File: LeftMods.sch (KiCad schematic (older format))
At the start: 8 parts

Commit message: Clean up some files
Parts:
- removed D60, D61, D62: D_Small, Diodes_SMD:D_SOD-123, symbol D_Small
- removed LM1, LM4: MX-1.5U, MX_Alps_Hybrid:MX-1.5U, symbol MX-1U
- removed LM2: MX-1U, MX_Alps_Hybrid:MX-1U, symbol MX-1U
- removed LM3: MX-1.25U, MX_Alps_Hybrid:MX-1.25U-FLIPPED, symbol MX-1U
- removed LM5: MX-1.5U, MX_Alps_Hybrid:MX-1.5U-FLIPPED, symbol MX-1U
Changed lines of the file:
@@
 LIBS:logic
 LIBS:Type-C
-LIBS:VoyagerII-cache
+LIBS:Voyager65-cache
 EELAYER 25 0
 EELAYER END
@@
 Comment4 ""
 $EndDescr
-$Comp
-L MX-1U LM1
-U 1 1 5A68E95B
-P 2325 2225
-F 0 "LM1" H 2325 2350 60  0000 C CNN
-F 1 "MX-1.5U" H 2325 2275 20  0000 C CNN
-F 2 "MX_Alps_Hybrid:MX-1.5U" H 2300 2200 60  0001 C CNN
-F 3 "" H 2300 2200 60  0001 C CNN
-	1    2325 2225
-	1    0    0    -1
-$EndComp
-$Comp
-L D_Small D60
-U 1 1 5A68E962
-P 2225 2500
-F 0 "D60" H 2175 2580 50  0000 L CNN
-F 1 "D_Small" H 2075 2420 50  0000 L CNN
-F 2 "Diodes_SMD:D_SOD-123" V 2225 2500 50  0001 C CNN
-F 3 "" V 2225 2500 50  0001 C CNN
-	1    2225 2500
-	0    -1   -1   0
-$EndComp
-$Comp
-L MX-1U LM2
-U 1 1 5A68E96A
-P 2775 2225
-F 0 "LM2" H 2775 2350 60  0000 C CNN
-F 1 "MX-1U" H 2775 2275 20  0000 C CNN
-F 2 "MX_Alps_Hybrid:MX-1U" H 2750 2200 60  0001 C CNN
-F 3 "" H 2750 2200 60  0001 C CNN
-	1    2775 2225
-	1    0    0    -1
-$EndComp
-$Comp
-L D_Small D61
-U 1 1 5A68E971
-P 2675 2500
-F 0 "D61" H 2625 2580 50  0000 L CNN
-F 1 "D_Small" H 2525 2420 50  0000 L CNN
-F 2 "Diodes_SMD:D_SOD-123" V 2675 2500 50  0001 C CNN
-F 3 "" V 2675 2500 50  0001 C CNN
-	1    2675 2500
-	0    -1   -1   0
-$EndComp
-Wire Wire Line
-	2600 2400 2750 2400
-$Comp
-L MX-1U LM4
-U 1 1 5A68E979
-P 3225 2225
-F 0 "LM4" H 3225 2350 60  0000 C CNN
-F 1 "MX-1.5U" H 3225 2275 20  0000 C CNN
-F 2 "MX_Alps_Hybrid:MX-1.5U" H 3200 2200 60  0001 C CNN
-F 3 "" H 3200 2200 60  0001 C CNN
-	1    3225 2225
-	1    0    0    -1
-$EndComp
-$Comp
-L D_Small D62
-U 1 1 5A68E980
-P 3125 2500
-F 0 "D62" H 3075 2580 50  0000 L CNN
-F 1 "D_Small" H 2975 2420 50  0000 L CNN
-F 2 "Diodes_SMD:D_SOD-123" V 3125 2500 50  0001 C CNN
-F 3 "" V 3125 2500 50  0001 C CNN
-	1    3125 2500
-	0    -1   -1   0
-$EndComp
-Wire Wire Line
-	3125 2400 3525 2400
-$Comp
-L MX-1U LM3
-U 1 1 5A68E997
-P 2775 2850
-F 0 "LM3" H 2775 2975 60  0000 C CNN
-F 1 "MX-1.25U" H 2775 2900 20  0000 C CNN
-F 2 "MX_Alps_Hybrid:MX-1.25U-FLIPPED" H 2750 2825 60  0001 C CNN
-F 3 "" H 2750 2825 60  0001 C CNN
-	1    2775 2850
-	1    0    0    -1
-$EndComp
-Wire Wire Line
-	2600 3025 2750 3025
-$Comp
-L MX-1U LM5
-U 1 1 5A68E9A6
-P 3225 2850
-F 0 "LM5" H 3225 2975 60  0000 C CNN
-F 1 "MX-1.5U" H 3225 2900 20  0000 C CNN
-F 2 "MX_Alps_Hybrid:MX-1.5U-FLIPPED" H 3200 2825 60  0001 C CNN
-F 3 "" H 3200 2825 60  0001 C CNN
-	1    3225 2850
-	1    0    0    -1
-$EndComp
-Connection ~ 3125 2400
-Wire Wire Line
-	2600 2400 2600 3025
-Connection ~ 2675 2400
-Text GLabel 2500 1700 1    60   Input ~ 0
-COL0
-Wire Wire Line
-	2950 1700 2950 2825
-Text GLabel 2950 1700 1    60   Input ~ 0
-COL1
-Wire Wire Line
-	3400 1700 3400 2675
-Text GLabel 3400 1700 1    60   Input ~ 0
-COL2
-Wire Wire Line
-	1700 2600 3125 2600
-Text GLabel 1700 2600 0    60   Input ~ 0
-ROW4
-Connection ~ 2225 2600
-Connection ~ 2675 2600
-Connection ~ 2950 2200
-Connection ~ 3400 2200
-Connection ~ 2800 2350
-Wire Wire Line
-	2500 1700 2500 2200
-Wire Wire Line
-	2225 2400 2300 2400
-Wire Wire Line
-	3400 2675 3200 2675
-Wire Wire Line
-	3200 2675 3200 3025
-Wire Wire Line
-	3525 2825 3400 2825
-Connection ~ 3200 2400
-Wire Wire Line
-	3525 2400 3525 2825
-Wire Wire Line
-	1750 2350 3250 2350
-Connection ~ 2350 2350
-Text GLabel 1750 2350 0    60   Input ~ 0
-LED-SW1
-Wire Wire Line
-	2450 2250 2450 1325
-Text GLabel 2450 1325 1    60   Input ~ 0
-LED-CS1
-Wire Wire Line
-	2900 1325 2900 2875
-Text GLabel 2900 1325 1    60   Input ~ 0
-LED-CS2
-Wire Wire Line
-	3350 1325 3350 2875
-Text GLabel 3350 1325 1    60   Input ~ 0
-LED-CS3
-Connection ~ 2900 2250
-Wire Wire Line
-	2800 2350 2800 2975
-Connection ~ 3350 2250
-Wire Wire Line
-	3250 2350 3250 2975
 $EndSCHEMATC

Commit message: Replace MCU, route bus
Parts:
- added D63, D64, D65: D_Small, Diodes_SMD:D_SOD-123, symbol D_Small
- added K_LM1, K_LM7: MX-1.5U, MX_Alps_Hybrid:MX-1.5U, symbol MX-1.5U
- added K_LM2: MX-1.25U, MX_Alps_Hybrid:MX-1.25U-FLIPPED, symbol MX-1.5U
- added K_LM3: MX-1.5U, MX_Alps_Hybrid:MX-1.5U-FLIPPED, symbol MX-1.5U
- added K_LM4, K_LM5, K_LM6: MX-1.25U, MX_Alps_Hybrid:MX-1.25U, symbol MX-1.5U
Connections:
- new net: D63.2 (A), K_LM1.2 (ROW)
- new net: D64.2 (A), K_LM3.2 (ROW), K_LM4.1 (COL)
- new net: D65.2 (A), K_LM6.2 (ROW), K_LM7.1 (COL)
- new net COL0: K_LM1.1 (COL), K_LM2.1 (COL)
- new net COL1: K_LM3.1 (COL), K_LM4.2 (ROW), K_LM5.1 (COL)
- new net COL2: K_LM6.1 (COL), K_LM7.2 (ROW)
- new net ROW4: D63.1 (K), D64.1 (K), D65.1 (K)
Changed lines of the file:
@@
 $Descr A4 11693 8268
 encoding utf-8
-Sheet 4 6
+Sheet 3 6
 Title ""
 Date ""
@@
 Comment4 ""
 $EndDescr
+$Comp
+L MX-1.5U K_LM1
+U 1 1 5ACD9BDC
+P 2225 2600
+F 0 "K_LM1" H 2225 2725 60  0000 C CNN
+F 1 "MX-1.5U" H 2225 2650 20  0000 C CNN
+F 2 "MX_Alps_Hybrid:MX-1.5U" H 2200 2575 60  0001 C CNN
+F 3 "" H 2200 2575 60  0001 C CNN
+	1    2225 2600
+	1    0    0    -1
+$EndComp
+$Comp
+L MX-1.5U K_LM2
+U 1 1 5ACD9C06
+P 2225 3200
+F 0 "K_LM2" H 2225 3325 60  0000 C CNN
+F 1 "MX-1.25U" H 2225 3250 20  0000 C CNN
+F 2 "MX_Alps_Hybrid:MX-1.25U-FLIPPED" H 2200 3175 60  0001 C CNN
+F 3 "" H 2200 3175 60  0001 C CNN
+	1    2225 3200
+	1    0    0    -1
+$EndComp
+$Comp
+L D_Small D63
+U 1 1 5ACD9CD9
+P 2125 2875
+F 0 "D63" H 2075 2955 50  0000 L CNN
+F 1 "D_Small" H 1975 2795 50  0000 L CNN
+F 2 "Diodes_SMD:D_SOD-123" V 2125 2875 50  0001 C CNN
+F 3 "" V 2125 2875 50  0001 C CNN
+	1    2125 2875
+	0    -1   -1   0
+$EndComp
+$Comp
+L MX-1.5U K_LM3
+U 1 1 5ACDA08B
+P 2750 2600
+F 0 "K_LM3" H 2750 2725 60  0000 C CNN
+F 1 "MX-1.5U" H 2750 2650 20  0000 C CNN
+F 2 "MX_Alps_Hybrid:MX-1.5U-FLIPPED" H 2725 2575 60  0001 C CNN
+F 3 "" H 2725 2575 60  0001 C CNN
+	1    2750 2600
+	1    0    0    -1
+$EndComp
+$Comp
+L MX-1.5U K_LM4
+U 1 1 5ACDA091
+P 2750 3200
+F 0 "K_LM4" H 2750 3325 60  0000 C CNN
+F 1 "MX-1.25U" H 2750 3250 20  0000 C CNN
+F 2 "MX_Alps_Hybrid:MX-1.25U" H 2725 3175 60  0001 C CNN
+F 3 "" H 2725 3175 60  0001 C CNN
+	1    2750 3200
+	1    0    0    -1
+$EndComp
+$Comp
+L D_Small D64
+U 1 1 5ACDA097
+P 2650 2875
+F 0 "D64" H 2600 2955 50  0000 L CNN
+F 1 "D_Small" H 2500 2795 50  0000 L CNN
+F 2 "Diodes_SMD:D_SOD-123" V 2650 2875 50  0001 C CNN
+F 3 "" V 2650 2875 50  0001 C CNN
+	1    2650 2875
+	0    -1   -1   0
+$EndComp
+$Comp
+L MX-1.5U K_LM5
+U 1 1 5ACDA0FC
+P 2750 3800
+F 0 "K_LM5" H 2750 3925 60  0000 C CNN
+F 1 "MX-1.25U" H 2750 3850 20  0000 C CNN
+F 2 "MX_Alps_Hybrid:MX-1.25U" H 2725 3775 60  0001 C CNN
+F 3 "" H 2725 3775 60  0001 C CNN
+	1    2750 3800
+	1    0    0    -1
+$EndComp
+$Comp
+L MX-1.5U K_LM6
+U 1 1 5ACDA22D
+P 3350 2600
+F 0 "K_LM6" H 3350 2725 60  0000 C CNN
+F 1 "MX-1.25U" H 3350 2650 20  0000 C CNN
+F 2 "MX_Alps_Hybrid:MX-1.25U" H 3325 2575 60  0001 C CNN
+F 3 "" H 3325 2575 60  0001 C CNN
+	1    3350 2600
+	1    0    0    -1
+$EndComp
+$Comp
+L MX-1.5U K_LM7
+U 1 1 5ACDA233
+P 3350 3200
+F 0 "K_LM7" H 3350 3325 60  0000 C CNN
+F 1 "MX-1.5U" H 3350 3250 20  0000 C CNN
+F 2 "MX_Alps_Hybrid:MX-1.5U" H 3325 3175 60  0001 C CNN
+F 3 "" H 3325 3175 60  0001 C CNN
+	1    3350 3200
+	1    0    0    -1
+$EndComp
+$Comp
+L D_Small D65
+U 1 1 5ACDA239
+P 3250 2875
+F 0 "D65" H 3200 2955 50  0000 L CNN
+F 1 "D_Small" H 3100 2795 50  0000 L CNN
+F 2 "Diodes_SMD:D_SOD-123" V 3250 2875 50  0001 C CNN
+F 3 "" V 3250 2875 50  0001 C CNN
+	1    3250 2875
+	0    -1   -1   0
+$EndComp
+Text GLabel 1925 2975 0    60   Input ~ 0
+ROW4
+Text GLabel 2400 2300 1    60   Input ~ 0
+COL0
+Text GLabel 2925 2300 1    60   Input ~ 0
+COL1
+Text GLabel 3525 2300 1    60   Input ~ 0
+COL2
+Connection ~ 3525 2575
+Connection ~ 2925 2575
+Wire Wire Line
+	2925 2300 2925 3125
+Wire Wire Line
+	2925 3225 2925 3775
+Connection ~ 2400 2575
+Wire Wire Line
+	2400 2300 2400 3175
+Connection ~ 2125 2975
+Connection ~ 2650 2975
+Wire Wire Line
+	1925 2975 3250 2975
+Wire Wire Line
+	3250 2775 3600 2775
+Wire Wire Line
+	2650 2775 2750 2775
+Wire Wire Line
+	2125 2775 2200 2775
+Wire Wire Line
+	3525 2300 3525 3075
+Wire Wire Line
+	3525 3075 3325 3075
+Wire Wire Line
+	3325 3075 3325 3375
+Wire Wire Line
+	3525 3175 3600 3175
+Wire Wire Line
+	3600 3175 3600 2775
+Connection ~ 3325 2775
+Wire Wire Line
+	2925 3125 2975 3125
+Wire Wire Line
+	2975 3125 2975 3225
+Wire Wire Line
+	2975 3225 2925 3225
+Wire Wire Line
+	2925 3175 2750 3175
+Wire Wire Line
+	2750 3175 2750 2775
+Connection ~ 2725 2775
+Wire Wire Line
+	2725 3375 2925 3375
+Connection ~ 2925 3375
 $EndSCHEMATC

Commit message: Temporary progress save
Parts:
- K_LM4: footprint MX_Alps_Hybrid:MX-1.25U -> MX_Alps_Hybrid:MX-1.25U-FLIPPED
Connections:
- net at D64.2 (A), K_LM3.2 (ROW), K_LM4.1 (COL): now also K_LM5.2 (ROW)
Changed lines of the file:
@@
 F 0 "K_LM4" H 2750 3325 60  0000 C CNN
 F 1 "MX-1.25U" H 2750 3250 20  0000 C CNN
-F 2 "MX_Alps_Hybrid:MX-1.25U" H 2725 3175 60  0001 C CNN
+F 2 "MX_Alps_Hybrid:MX-1.25U-FLIPPED" H 2725 3175 60  0001 C CNN
 F 3 "" H 2725 3175 60  0001 C CNN
 	1    2750 3200
@@
 	3250 2775 3600 2775
 Wire Wire Line
-	2650 2775 2750 2775
+	2525 2775 2750 2775
 Wire Wire Line
 	2125 2775 2200 2775
@@
 	2725 3375 2925 3375
 Connection ~ 2925 3375
+Wire Wire Line
+	2725 3975 2725 3475
+Wire Wire Line
+	2725 3475 2525 3475
+Wire Wire Line
+	2525 3475 2525 2775
+Connection ~ 2650 2775
 $EndSCHEMATC

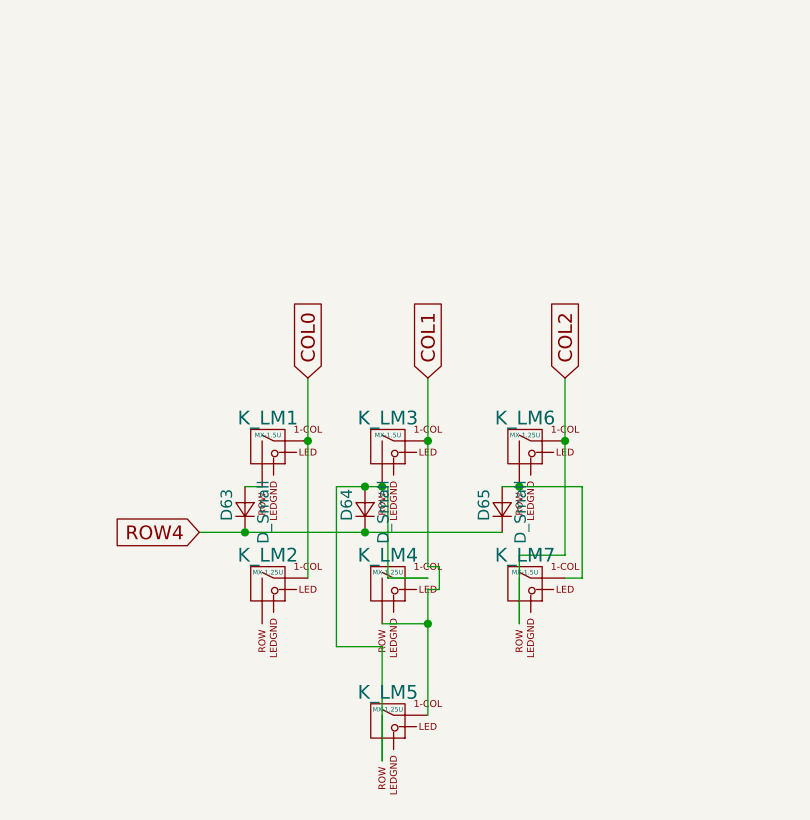
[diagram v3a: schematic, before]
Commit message: Finish project basic routing
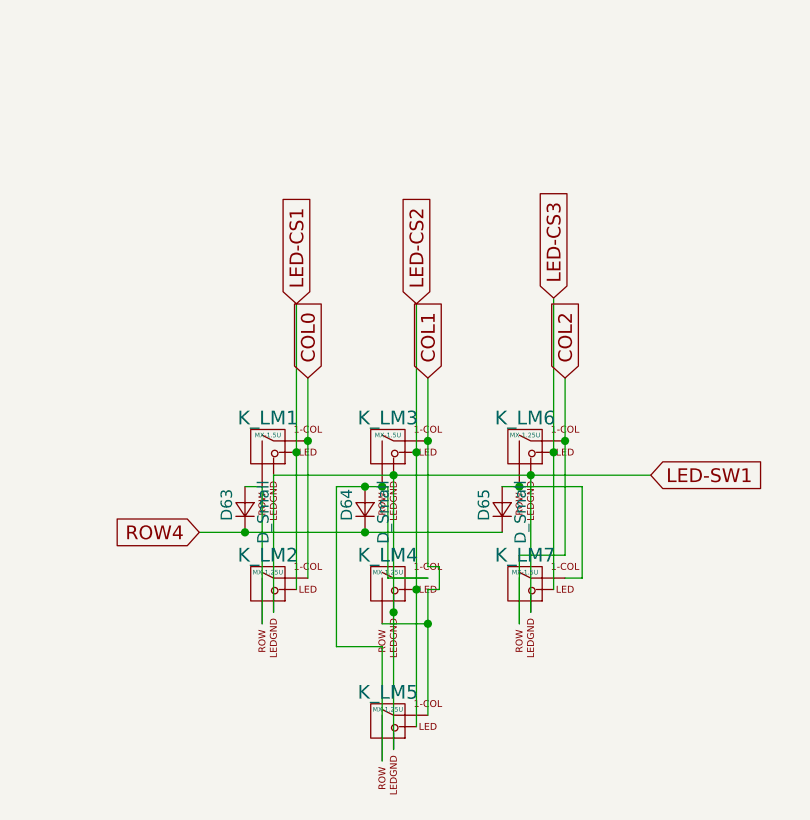
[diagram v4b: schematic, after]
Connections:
- net at D63.2 (A), K_LM1.2 (ROW): now also K_LM2.2 (ROW)
- net LED-CS1: now reaches K_LM1.3 (LED)
- net LED-CS1: now also K_LM2.3 (LED)
- net LED-SW1: now reaches K_LM1.4 (LEDGND)
- net LED-SW1: now also K_LM2.4 (LEDGND), K_LM3.4 (LEDGND), K_LM4.4 (LEDGND), K_LM5.4 (LEDGND), K_LM6.4 (LEDGND), K_LM7.4 (LEDGND)
- net LED-CS2: now reaches K_LM3.3 (LED)
- net LED-CS2: now also K_LM4.3 (LED), K_LM5.3 (LED)
- net LED-CS3: now reaches K_LM6.3 (LED)
- net LED-CS3: now also K_LM7.3 (LED)
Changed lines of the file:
@@
 	2525 3475 2525 2775
 Connection ~ 2650 2775
+Wire Wire Line
+	2350 1975 2350 3225
+Connection ~ 2350 2625
+Text GLabel 2350 1975 1    60   Input ~ 0
+LED-CS1
+Wire Wire Line
+	2250 2725 3900 2725
+Connection ~ 2775 2725
+Connection ~ 3375 2725
+Text GLabel 3900 2725 2    60   Input ~ 0
+LED-SW1
+Wire Wire Line
+	3375 3325 3375 2725
+Wire Wire Line
+	2775 2725 2775 3925
+Connection ~ 2775 3325
+Wire Wire Line
+	2250 3325 2250 2725
+Wire Wire Line
+	2200 2775 2200 3375
+Wire Wire Line
+	2875 1975 2875 3825
+Text GLabel 2875 1975 1    60   Input ~ 0
+LED-CS2
+Wire Wire Line
+	3475 1950 3475 3225
+Text GLabel 3475 1950 1    60   Input ~ 0
+LED-CS3
+Connection ~ 2875 2625
+Connection ~ 3475 2625
+Connection ~ 2875 3225
 $EndSCHEMATC

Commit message: Low cost edition complete
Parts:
- K_LM1, K_LM7: footprint MX_Alps_Hybrid:MX-1.5U -> MX_Alps_Hybrid:MX-1.5U-NoLED
- K_LM2, K_LM4: footprint MX_Alps_Hybrid:MX-1.25U-FLIPPED -> MX_Alps_Hybrid:MX-1.25U-NoLED
- K_LM3: footprint MX_Alps_Hybrid:MX-1.5U-FLIPPED -> MX_Alps_Hybrid:MX-1.5U-NoLED
- K_LM5, K_LM6: footprint MX_Alps_Hybrid:MX-1.25U -> MX_Alps_Hybrid:MX-1.25U-NoLED
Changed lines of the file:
@@
 F 0 "K_LM1" H 2225 2725 60  0000 C CNN
 F 1 "MX-1.5U" H 2225 2650 20  0000 C CNN
-F 2 "MX_Alps_Hybrid:MX-1.5U" H 2200 2575 60  0001 C CNN
+F 2 "MX_Alps_Hybrid:MX-1.5U-NoLED" H 2200 2575 60  0001 C CNN
 F 3 "" H 2200 2575 60  0001 C CNN
 	1    2225 2600
@@
 F 0 "K_LM2" H 2225 3325 60  0000 C CNN
 F 1 "MX-1.25U" H 2225 3250 20  0000 C CNN
-F 2 "MX_Alps_Hybrid:MX-1.25U-FLIPPED" H 2200 3175 60  0001 C CNN
+F 2 "MX_Alps_Hybrid:MX-1.25U-NoLED" H 2200 3175 60  0001 C CNN
 F 3 "" H 2200 3175 60  0001 C CNN
 	1    2225 3200
@@
 F 0 "K_LM3" H 2750 2725 60  0000 C CNN
 F 1 "MX-1.5U" H 2750 2650 20  0000 C CNN
-F 2 "MX_Alps_Hybrid:MX-1.5U-FLIPPED" H 2725 2575 60  0001 C CNN
+F 2 "MX_Alps_Hybrid:MX-1.5U-NoLED" H 2725 2575 60  0001 C CNN
 F 3 "" H 2725 2575 60  0001 C CNN
 	1    2750 2600
@@
 F 0 "K_LM4" H 2750 3325 60  0000 C CNN
 F 1 "MX-1.25U" H 2750 3250 20  0000 C CNN
-F 2 "MX_Alps_Hybrid:MX-1.25U-FLIPPED" H 2725 3175 60  0001 C CNN
+F 2 "MX_Alps_Hybrid:MX-1.25U-NoLED" H 2725 3175 60  0001 C CNN
 F 3 "" H 2725 3175 60  0001 C CNN
 	1    2750 3200
@@
 F 0 "K_LM5" H 2750 3925 60  0000 C CNN
 F 1 "MX-1.25U" H 2750 3850 20  0000 C CNN
-F 2 "MX_Alps_Hybrid:MX-1.25U" H 2725 3775 60  0001 C CNN
+F 2 "MX_Alps_Hybrid:MX-1.25U-NoLED" H 2725 3775 60  0001 C CNN
 F 3 "" H 2725 3775 60  0001 C CNN
 	1    2750 3800
@@
 F 0 "K_LM6" H 3350 2725 60  0000 C CNN
 F 1 "MX-1.25U" H 3350 2650 20  0000 C CNN
-F 2 "MX_Alps_Hybrid:MX-1.25U" H 3325 2575 60  0001 C CNN
+F 2 "MX_Alps_Hybrid:MX-1.25U-NoLED" H 3325 2575 60  0001 C CNN
 F 3 "" H 3325 2575 60  0001 C CNN
 	1    3350 2600
@@
 F 0 "K_LM7" H 3350 3325 60  0000 C CNN
 F 1 "MX-1.5U" H 3350 3250 20  0000 C CNN
-F 2 "MX_Alps_Hybrid:MX-1.5U" H 3325 3175 60  0001 C CNN
+F 2 "MX_Alps_Hybrid:MX-1.5U-NoLED" H 3325 3175 60  0001 C CNN
 F 3 "" H 3325 3175 60  0001 C CNN
 	1    3350 3200
